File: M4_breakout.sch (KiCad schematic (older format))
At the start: 58 parts, among them P1 CONN_01X02, P2 CONN_01X16, P3 CONN_01X16, SW1 SPST, SW2 QDIPSW, U1 LP2985LV, U2 STM32F318K8

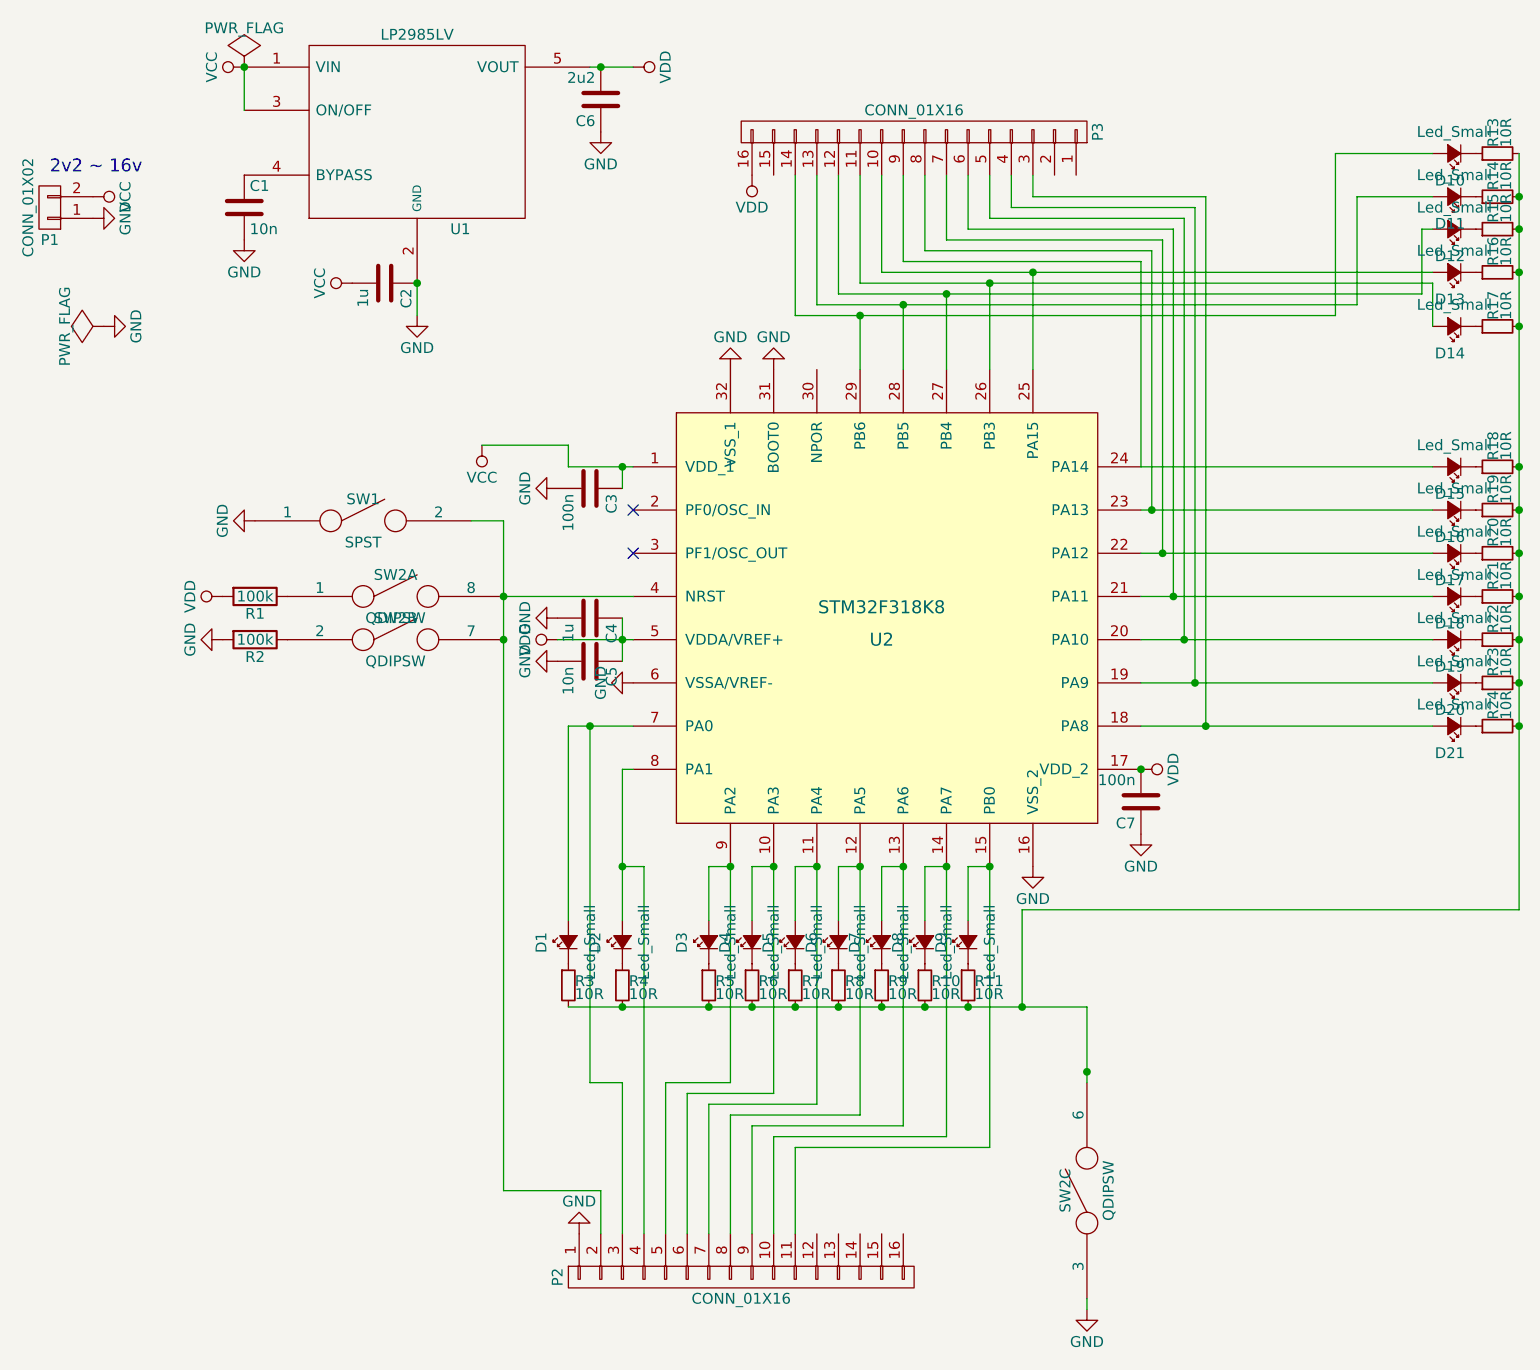
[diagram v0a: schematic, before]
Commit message: proper reset
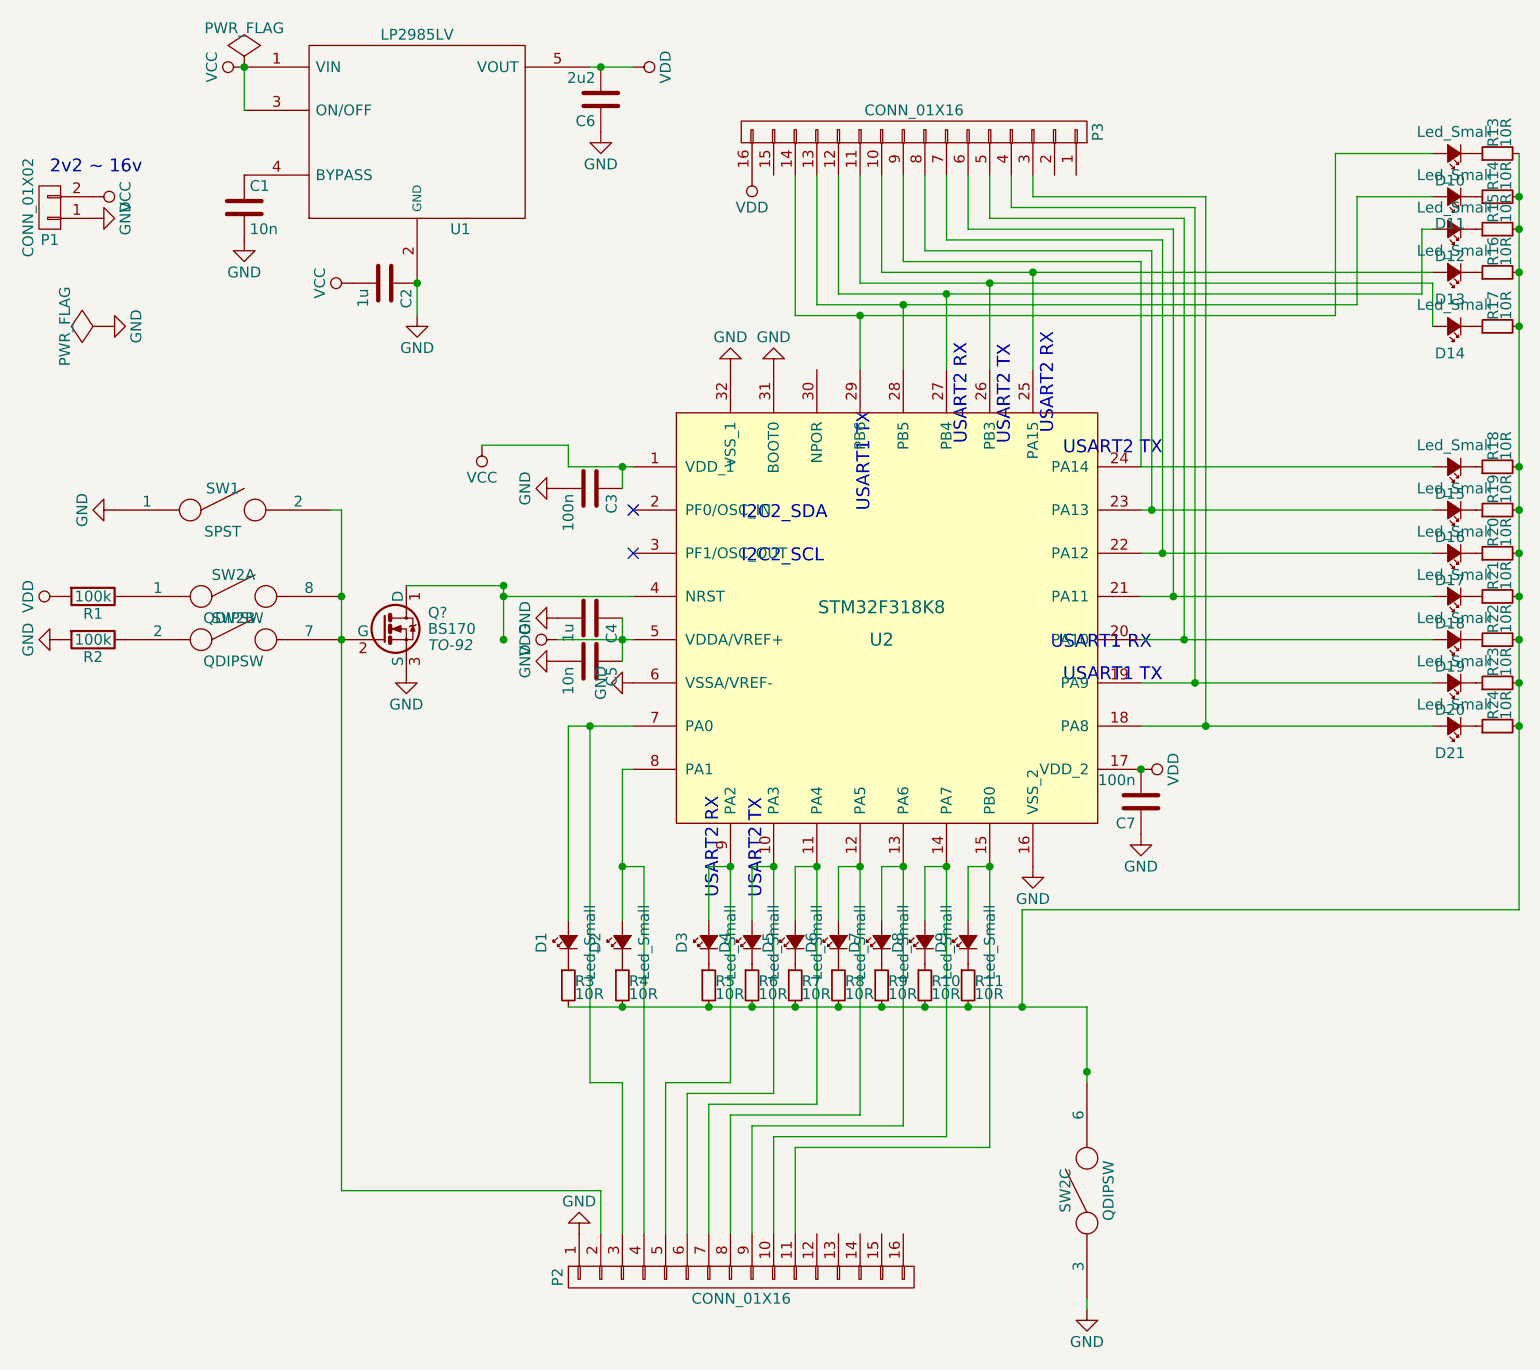
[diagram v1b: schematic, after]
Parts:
- added Q?: BS170, TO-92, symbol BS170
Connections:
- net GND: now also Q?.3 (S)
- net at P2.2 (P2), SW1.2, SW2.7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: now also Q?.2 (G); no longer U2.4 (NRST)
- new net: Q?.1 (D), U2.4 (NRST)
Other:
- note added: "I2C2_SCL"
- note added: "I2C2_SDA"
- note added: "USART1 RX"
- note added: "USART1 TX"
- note added: "USART2 RX"
- note added: "USART2 TX"
- moved on the sheet: R1, R2, SW1, SW2A, SW2B
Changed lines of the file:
@@
 	3350 3600 2750 3600
 Wire Wire Line
-	2750 3250 2750 6350
-Wire Wire Line
-	2750 6350 3200 6350
+	2000 6350 3200 6350
 Wire Wire Line
 	3200 6350 3200 6550
@@
 L R R1
 U 1 1 57B7CB16
-P 1600 3600
-F 0 "R1" V 1680 3600 50  0000 C CNN
-F 1 "100k" V 1600 3600 50  0000 C CNN
-F 2 "Resistors_SMD:R_0805" V 1530 3600 50  0001 C CNN
-F 3 "" H 1600 3600 50  0000 C CNN
-	1    1600 3600
+P 850 3600
+F 0 "R1" V 930 3600 50  0000 C CNN
+F 1 "100k" V 850 3600 50  0000 C CNN
+F 2 "Resistors_SMD:R_0805" V 780 3600 50  0001 C CNN
+F 3 "" H 850 3600 50  0000 C CNN
+	1    850  3600
 	0    1    1    0
 $EndComp
@@
 L R R2
 U 1 1 57B7D106
-P 1600 3800
-F 0 "R2" V 1680 3800 50  0000 C CNN
-F 1 "100k" V 1600 3800 50  0000 C CNN
-F 2 "Resistors_SMD:R_0805" V 1530 3800 50  0001 C CNN
-F 3 "" H 1600 3800 50  0000 C CNN
-	1    1600 3800
+P 850 3800
+F 0 "R2" V 930 3800 50  0000 C CNN
+F 1 "100k" V 850 3800 50  0000 C CNN
+F 2 "Resistors_SMD:R_0805" V 780 3800 50  0001 C CNN
+F 3 "" H 850 3800 50  0000 C CNN
+	1    850  3800
 	0    1    1    0
 $EndComp
@@
 L VDD #PWR023
 U 1 1 57B7D1D3
-P 1450 3600
-F 0 "#PWR023" H 1450 3450 50  0001 C CNN
-F 1 "VDD" H 1450 3750 50  0000 C CNN
-F 2 "" H 1450 3600 50  0000 C CNN
-F 3 "" H 1450 3600 50  0000 C CNN
-	1    1450 3600
+P 700 3600
+F 0 "#PWR023" H 700 3450 50  0001 C CNN
+F 1 "VDD" H 700 3750 50  0000 C CNN
+F 2 "" H 700 3600 50  0000 C CNN
+F 3 "" H 700 3600 50  0000 C CNN
+	1    700  3600
 	0    -1   -1   0
 $EndComp
@@
 L GND #PWR024
 U 1 1 57B7D288
-P 1450 3800
-F 0 "#PWR024" H 1450 3550 50  0001 C CNN
-F 1 "GND" H 1450 3650 50  0000 C CNN
-F 2 "" H 1450 3800 50  0000 C CNN
-F 3 "" H 1450 3800 50  0000 C CNN
-	1    1450 3800
+P 700 3800
+F 0 "#PWR024" H 700 3550 50  0001 C CNN
+F 1 "GND" H 700 3650 50  0000 C CNN
+F 2 "" H 700 3800 50  0000 C CNN
+F 3 "" H 700 3800 50  0000 C CNN
+	1    700  3800
 	0    1    1    0
 $EndComp
@@
 $Comp
 L QDIPSW SW2
-U 1 1 57BC3C8E
-P 2250 3600
-F 0 "SW2" H 2250 3700 50  0000 C CNN
-F 1 "QDIPSW" H 2250 3500 50  0000 C CNN
-F 2 "Housings_SOIC:SOIC-8_3.9x4.9mm_Pitch1.27mm" H 2250 3600 50  0001 C CNN
-F 3 "" H 2250 3600 50  0000 C CNN
-	1    2250 3600
-	1    0    0    -1
-$EndComp
-$Comp
-L QDIPSW SW2
-U 2 1 57BC43B0
-P 2250 3800
-F 0 "SW2" H 2250 3900 50  0000 C CNN
-F 1 "QDIPSW" H 2250 3700 50  0000 C CNN
-F 2 "Housings_SOIC:SOIC-8_3.9x4.9mm_Pitch1.27mm" H 2250 3800 50  0001 C CNN
-F 3 "" H 2250 3800 50  0000 C CNN
-	2    2250 3800
-	1    0    0    -1
-$EndComp
-$Comp
-L QDIPSW SW2
 U 3 1 57BC49C2
 P 5450 6350
@@
 L SPST SW1
 U 1 1 57BC5E3A
-P 2100 3250
-F 0 "SW1" H 2100 3350 50  0000 C CNN
-F 1 "SPST" H 2100 3150 50  0000 C CNN
-F 2 "TO_SOT_Packages_SMD:SOT-543" H 2100 3250 50  0001 C CNN
-F 3 "" H 2100 3250 50  0000 C CNN
-	1    2100 3250
+P 1450 3200
+F 0 "SW1" H 1450 3300 50  0000 C CNN
+F 1 "SPST" H 1450 3100 50  0000 C CNN
+F 2 "TO_SOT_Packages_SMD:SOT-543" H 1450 3200 50  0001 C CNN
+F 3 "" H 1450 3200 50  0000 C CNN
+	1    1450 3200
 	1    0    0    -1
 $EndComp
-Wire Wire Line
-	2600 3250 2750 3250
 $Comp
 L GND #PWR025
 U 1 1 57BC6A05
-P 1600 3250
-F 0 "#PWR025" H 1600 3000 50  0001 C CNN
-F 1 "GND" H 1600 3100 50  0000 C CNN
-F 2 "" H 1600 3250 50  0000 C CNN
-F 3 "" H 1600 3250 50  0000 C CNN
-	1    1600 3250
+P 950 3200
+F 0 "#PWR025" H 950 2950 50  0001 C CNN
+F 1 "GND" H 950 3050 50  0000 C CNN
+F 2 "" H 950 3200 50  0000 C CNN
+F 3 "" H 950 3200 50  0000 C CNN
+	1    950  3200
 	0    1    1    0
 $EndComp
@@
 	7050 2150 7050 2350
 Connection ~ 5000 2150
+Text Notes 3750 5000 1    60   ~ 0
+USART2 RX
+Text Notes 3950 5000 1    60   ~ 0
+USART2 TX
+Text Notes 5750 3850 2    60   ~ 0
+USART1 RX
+Text Notes 5800 4000 2    60   ~ 0
+USART1 TX
+Text Notes 5300 2850 1    60   ~ 0
+USART2 RX
+Text Notes 5100 2900 1    60   ~ 0
+USART2 TX
+Text Notes 4450 2750 3    60   ~ 0
+USART1 TX
+Text Notes 4900 2900 1    60   ~ 0
+USART2 RX
+Text Notes 5800 2950 2    60   ~ 0
+USART2 TX
+Text Notes 3850 3250 0    60   ~ 0
+I2C2_SDA
+Text Notes 3850 3450 0    60   ~ 0
+I2C2_SCL
+$Comp
+L QDIPSW SW2
+U 2 1 57BC43B0
+P 1500 3800
+F 0 "SW2" H 1500 3900 50  0000 C CNN
+F 1 "QDIPSW" H 1500 3700 50  0000 C CNN
+F 2 "Housings_SOIC:SOIC-8_3.9x4.9mm_Pitch1.27mm" H 1500 3800 50  0001 C CNN
+F 3 "" H 1500 3800 50  0000 C CNN
+	2    1500 3800
+	1    0    0    -1
+$EndComp
+$Comp
+L QDIPSW SW2
+U 1 1 57BC3C8E
+P 1500 3600
+F 0 "SW2" H 1500 3700 50  0000 C CNN
+F 1 "QDIPSW" H 1500 3500 50  0000 C CNN
+F 2 "Housings_SOIC:SOIC-8_3.9x4.9mm_Pitch1.27mm" H 1500 3600 50  0001 C CNN
+F 3 "" H 1500 3600 50  0000 C CNN
+	1    1500 3600
+	1    0    0    -1
+$EndComp
+$Comp
+L BS170 Q?
+U 1 1 57BDD85C
+P 2200 3750
+F 0 "Q?" H 2400 3825 50  0000 L CNN
+F 1 "BS170" H 2400 3750 50  0000 L CNN
+F 2 "TO-92" H 2400 3675 50  0000 L CIN
+F 3 "" H 2200 3750 50  0000 L CNN
+	1    2200 3750
+	1    0    0    -1
+$EndComp
+$Comp
+L GND #PWR?
+U 1 1 57BDDC54
+P 2300 3950
+F 0 "#PWR?" H 2300 3700 50  0001 C CNN
+F 1 "GND" H 2300 3800 50  0000 C CNN
+F 2 "" H 2300 3950 50  0000 C CNN
+F 3 "" H 2300 3950 50  0000 C CNN
+	1    2300 3950
+	1    0    0    -1
+$EndComp
+Wire Wire Line
+	2750 3550 2300 3550
+Connection ~ 2750 3550
+Wire Wire Line
+	2000 3200 1950 3200
+Wire Wire Line
+	2000 3200 2000 6350
+Connection ~ 2000 3600
+Wire Wire Line
+	2750 3550 2750 3800
+Connection ~ 2000 3800
 $EndSCHEMATC
